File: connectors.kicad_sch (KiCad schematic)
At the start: 6 parts, among them J4 SS5-10-3.00-L-D-K-TR, J5 EHF-105-01-L-D-SM-P-TR, J6 52746-0871, J7 DF52-2S-0.8H(21)

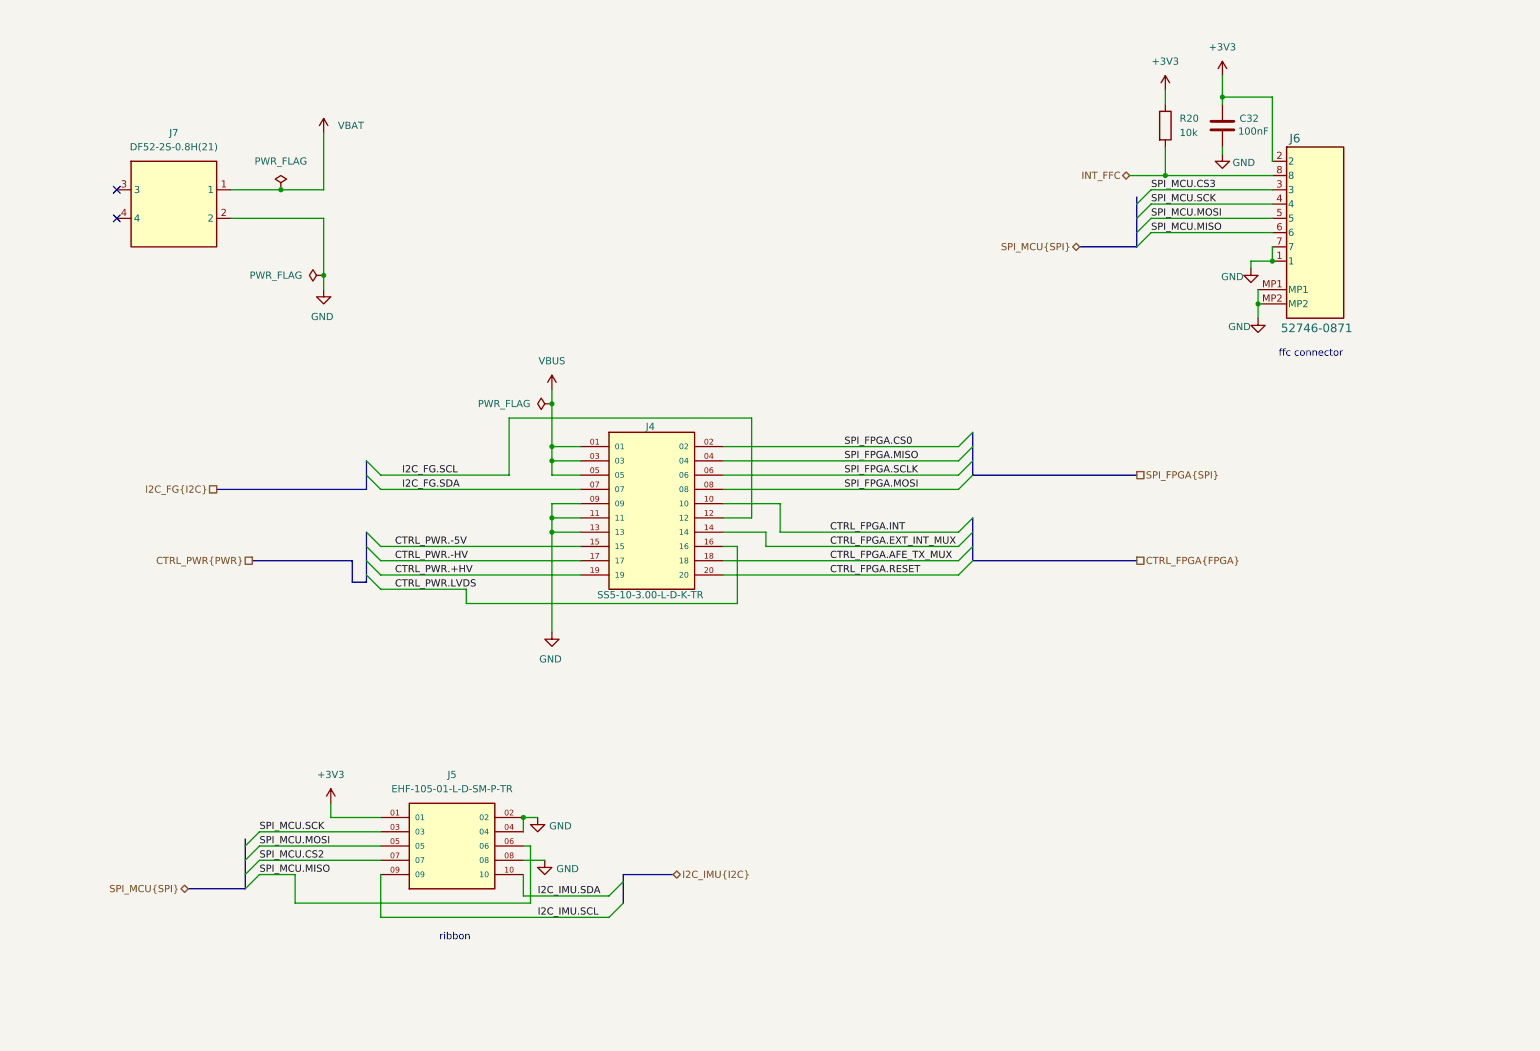
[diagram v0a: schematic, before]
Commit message: added schematics comments of review 1
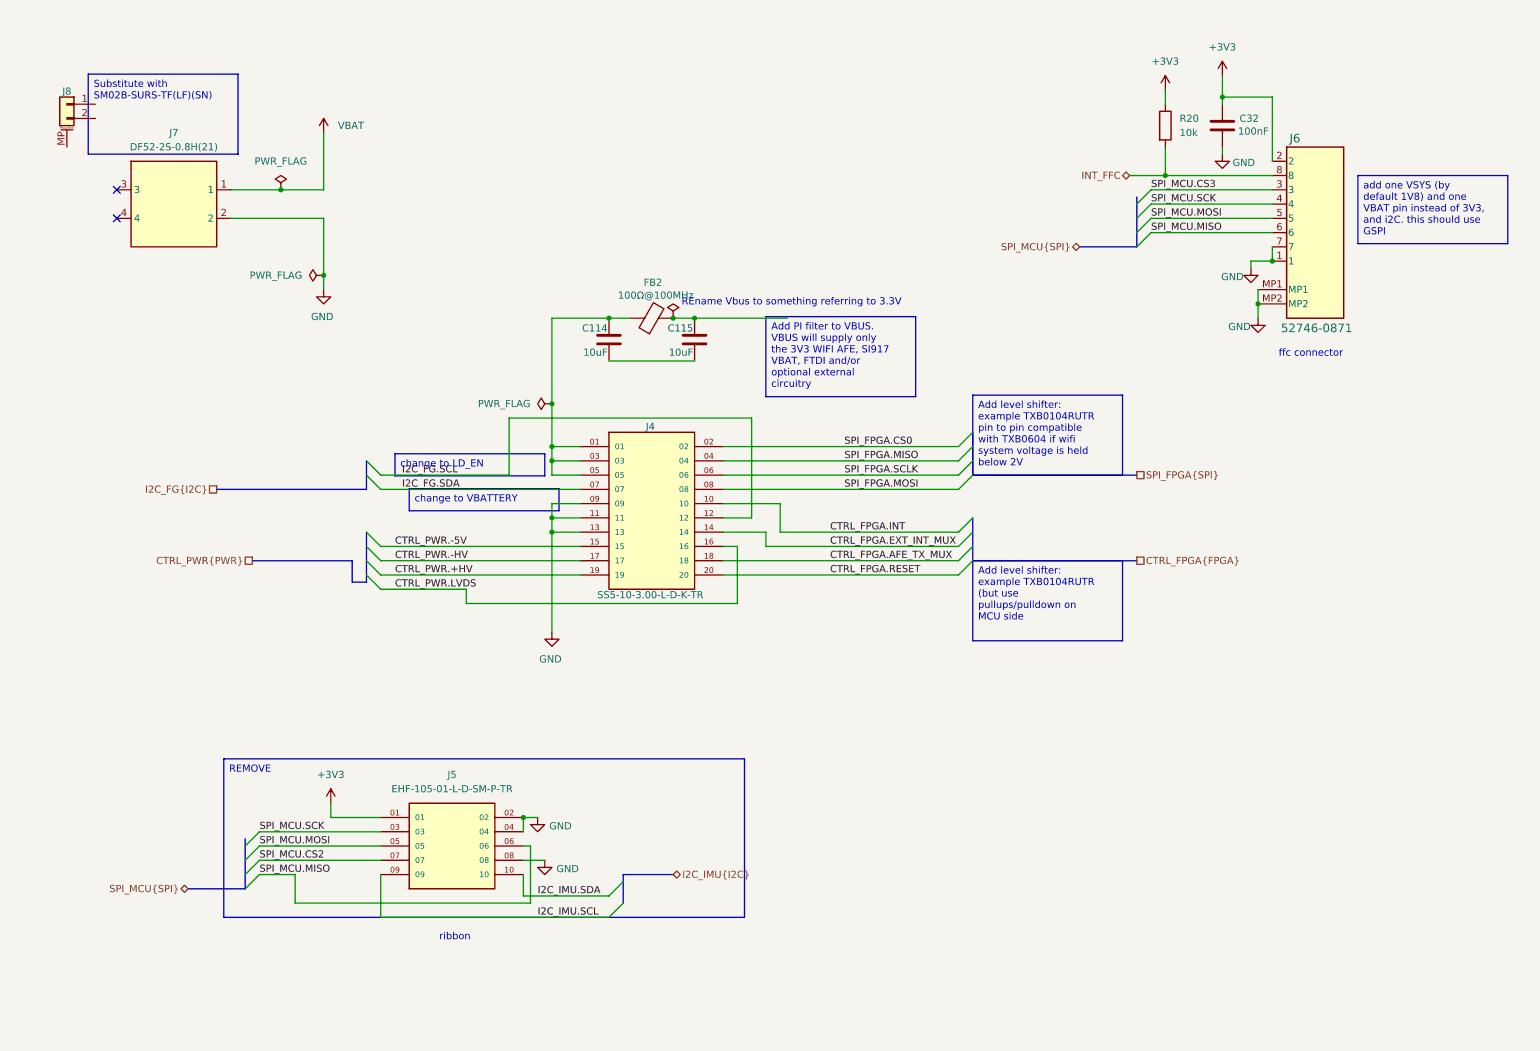
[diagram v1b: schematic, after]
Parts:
- added C114, C115: 10uF, Capacitor_SMD:C_0402_1005Metric, symbol #dzdb:g_cap/C-10u-0402
- added FB2: 100Ω@100MHz, Inductor_SMD:L_0603_1608Metric, symbol #dzdb:s_ind/L-MUR-BLM18SP101SN1
- added J8: 2, Connector_JST:JST_SUR_SM02B-SURS-TF_1x02-1MP_P0.80mm_Horizontal, symbol #gplm:con/CON-0033-0002
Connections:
- net VBUS: no longer names the net of J4.01, J4.03, J4.05
- net VBUS: now also C114.1, FB2.1
- new net: C114.2, C115.2
- new net: C115.1, FB2.2
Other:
- note added: "REname Vbus to something referring to 3.3V"

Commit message: changes after first review: add lvl shifters, board at 1v8, new power tree
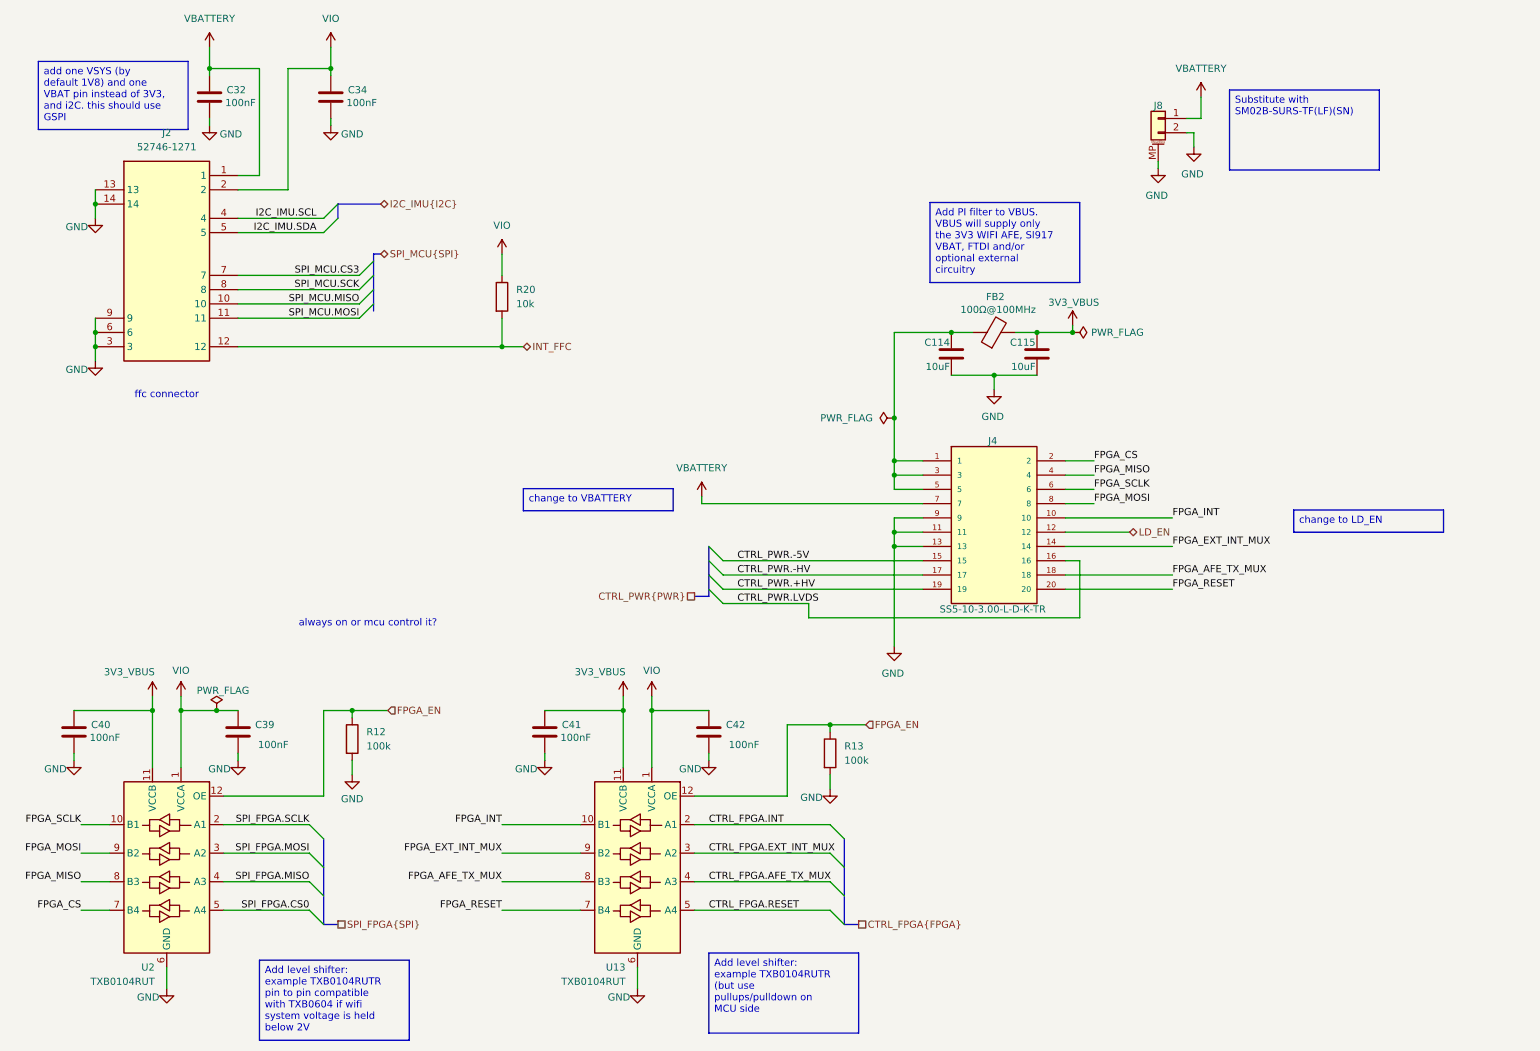
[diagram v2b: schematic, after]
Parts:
- removed J5: EHF-105-01-L-D-SM-P-TR, dz_con:SAMTEC_EHF-105-01-L-D-SM, symbol #dzdb:s_con/CON-SAM-EHF-105-01-L-D-SM-P-TR
- removed J6: 52746-0871, dz_con:CON_527460871_MOL, symbol #dzdb:s_con/CON-MOLEX-52746-0871
- removed J7: DF52-2S-0.8H(21), dz_con:DF522S08H21, symbol #dzdb:s_con/CON-HIROSE-DF52-2S-0.8H(21)
- added C34, C39, C40, C41, C42: 100nF, Capacitor_SMD:C_0603_1608Metric, symbol #dzdb:g_cap/C-100n-0603
- added J2: 52746-1271, dz_con:527461271, symbol #dzdb:s_con/CON-MOLEX-52746-1271
- added R12, R13: 100k, Resistor_SMD:R_0402_1005Metric, symbol #dzdb:g_res/R-100k-0402
- added U13, U2: TXB0104RUT, Package_DFN_QFN:Texas_R-PUQFN-N12, symbol Logic_LevelTranslator:TXB0104RUT
- J4: footprint dz_con:SAMTEC_SS5_10_3.00_X_D_K_XX -> dz_comm:QFN-56_FT232HPQ_FTD
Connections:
- net CTRL_FPGA.AFE_TX_MUX: now also U13.4 (A3); no longer J4.18
- net CTRL_FPGA.EXT_INT_MUX: now also U13.3 (A2); no longer J4.14
- net CTRL_FPGA.INT: now also U13.2 (A1); no longer J4.10
- net CTRL_FPGA.RESET: now also U13.5 (A4); no longer J4.20
- net GND: now also C114.2, C115.2, J4.9, J8.2 (Pin_2), J8.MP (MountPin), C34.2, C39.2, C40.2, C41.2, C42.2, J2.13, J2.14, J2.3, J2.6, J2.9, R12.2, R13.2, U13.6 (GND), U2.6 (GND); no longer J4.09
- net I2C_IMU.SCL: now also J2.4
- net I2C_IMU.SDA: now also J2.5
- net INT_FFC: now also J2.12
- net SPI_FPGA.CS0: now also U2.5 (A4); no longer J4.02
- net SPI_FPGA.MISO: now also U2.4 (A3); no longer J4.04
- net SPI_FPGA.MOSI: now also U2.3 (A2); no longer J4.08
- net SPI_FPGA.SCLK: now also U2.2 (A1); no longer J4.06
- net SPI_MCU.CS3: now also J2.7
- net SPI_MCU.MISO: now also J2.10
- net SPI_MCU.MOSI: now also J2.11
- net SPI_MCU.SCK: now also J2.8
- net VBATTERY: now reaches J8.1 (Pin_1)
- net VBATTERY: now also C32.1, J4.7, J2.1
- net 3V3_VBUS: now reaches C115.1, FB2.2
- net 3V3_VBUS: now also C40.1, C41.1, U13.11 (VCCB), U2.11 (VCCB)
- net +3V3 renamed VIO
- net VIO: now also C34.1, C39.1, C42.1, J2.2, U13.1 (VCCA), U2.1 (VCCA); no longer C32.1
- net I2C_FG.SCL renamed LD_EN
- removed net I2C_FG.SDA: J4.07
- new net: C114.1, FB2.1, J4.1, J4.3, J4.5
- new net FPGA_AFE_TX_MUX: J4.18, U13.8 (B3)
- new net FPGA_CS: J4.2, U2.7 (B4)
- new net FPGA_EN: R12.1, R13.1, U13.12 (OE), U2.12 (OE)
- new net FPGA_EXT_INT_MUX: J4.14, U13.9 (B2)
- new net FPGA_INT: J4.10, U13.10 (B1)
- new net FPGA_MISO: J4.4, U2.8 (B3)
- new net FPGA_MOSI: J4.8, U2.9 (B2)
- new net FPGA_RESET: J4.20, U13.7 (B4)
- new net FPGA_SCLK: J4.6, U2.10 (B1)
- no-connect marks 2 -> 0
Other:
- note added: "always on or mcu control it?"
- note removed: "REname Vbus to something referring to 3.3V"
- note removed: "ribbon"
- moved on the sheet: C114, C115, C32, FB2, J4, J8, R20

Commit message: updated schematic and initial pcb placement
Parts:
- removed R12: 100k, Resistor_SMD:R_0402_1005Metric, symbol #dzdb:g_res/R-100k-0402
- added M1, M2, M3, M4: MountingHole_Pad, dz_mech:MountingHole_2.4mm_M2_Pad_TopBottom, symbol #gplm:art/ART-0002-0002
- added R25: 100k, Resistor_SMD:R_0402_1005Metric, symbol #dzdb:g_res/R-100k-0402
- J4: footprint dz_comm:QFN-56_FT232HPQ_FTD -> dz_con:SAMTEC_SS5_10_3.00_X_D_K_XX
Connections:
- net SPI_FPGA.SCLK is gone; now on net SPI_FPGA.MISO: U2.2 (A1)
- net CTRL_FPGA.AFE_TX_MUX: now also U13.3 (A2); no longer U13.4 (A3)
- net CTRL_FPGA.EXT_INT_MUX: now also U13.4 (A3); no longer U13.3 (A2)
- net CTRL_FPGA.INT: now also U13.5 (A4); no longer U13.2 (A1)
- net CTRL_FPGA.RESET: now also U13.2 (A1); no longer U13.5 (A4)
- net FPGA_AFE_TX_MUX: now also U13.9 (B2); no longer U13.8 (B3)
- net FPGA_CS: now also U2.8 (B3); no longer U2.7 (B4)
- net FPGA_EXT_INT_MUX: now also U13.8 (B3); no longer U13.9 (B2)
- net FPGA_INT: now also U13.7 (B4); no longer U13.10 (B1)
- net FPGA_MISO: now also U2.10 (B1); no longer U2.8 (B3)
- net FPGA_MOSI: now also U2.7 (B4); no longer U2.9 (B2)
- net FPGA_RESET: now also U13.10 (B1); no longer U13.7 (B4)
- net FPGA_SCLK: now also U2.9 (B2); no longer U2.10 (B1)
- net LD_EN: now also R25.2
- net SPI_FPGA.CS0: now also U2.4 (A3); no longer U2.5 (A4)
- net SPI_FPGA.MISO: no longer U2.4 (A3)
- net SPI_FPGA.MOSI: now also U2.5 (A4); no longer U2.3 (A2)
- net VBATTERY: now also R25.1
- net SPI_MCU.CS3 renamed ULP_SSI.CS0
- net SPI_MCU.MISO renamed ULP_SSI.MISO
- net SPI_MCU.MOSI renamed ULP_SSI.MOSI
- net SPI_MCU.SCK renamed ULP_SSI.SCK
- new net GNDA: M1.1, M2.1
- new net SPI_FPGA.SCK: U2.3 (A2)
- no-connect marks 0 -> 2
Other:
- note removed: "always on or mcu control it?"
